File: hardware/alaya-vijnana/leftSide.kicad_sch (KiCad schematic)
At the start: 46 parts, among them J1 Bat, J2 USB_C_Receptacle_USB2.0_16P, SW1 Power_Switch, U1 nRF52840, U2 BQ24075RGT, U3 XC6220B331MR, X1 32.768kHz, Y1 32Mhz

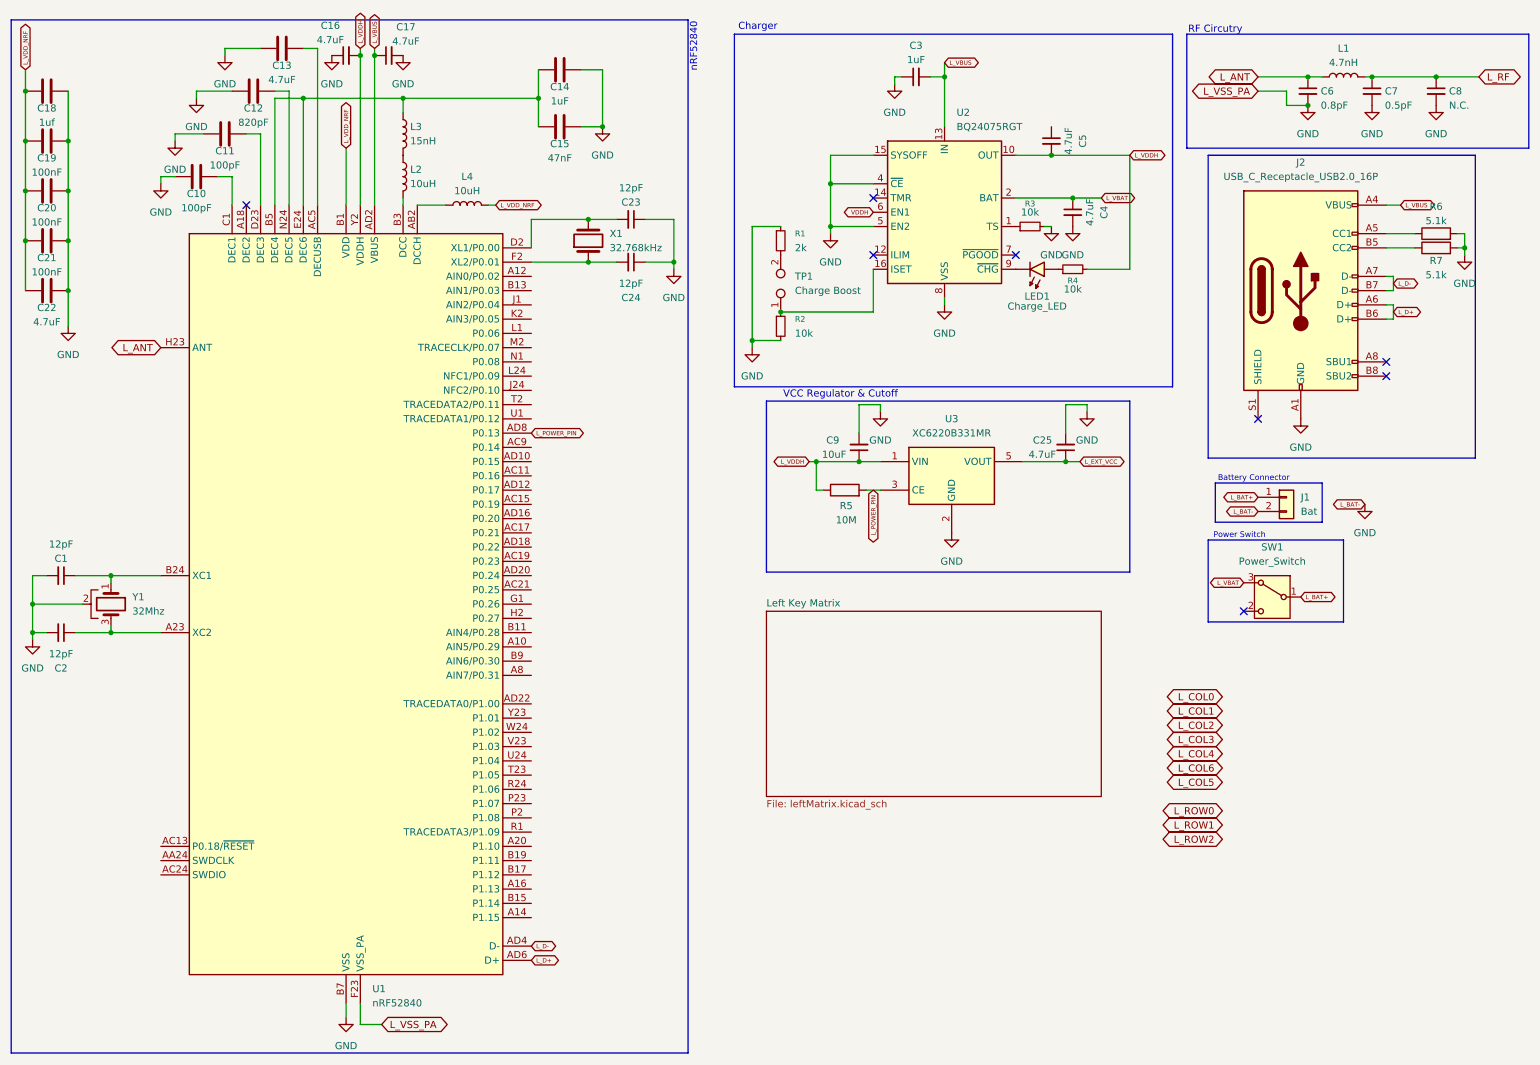
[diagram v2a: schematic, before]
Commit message: left side wired up
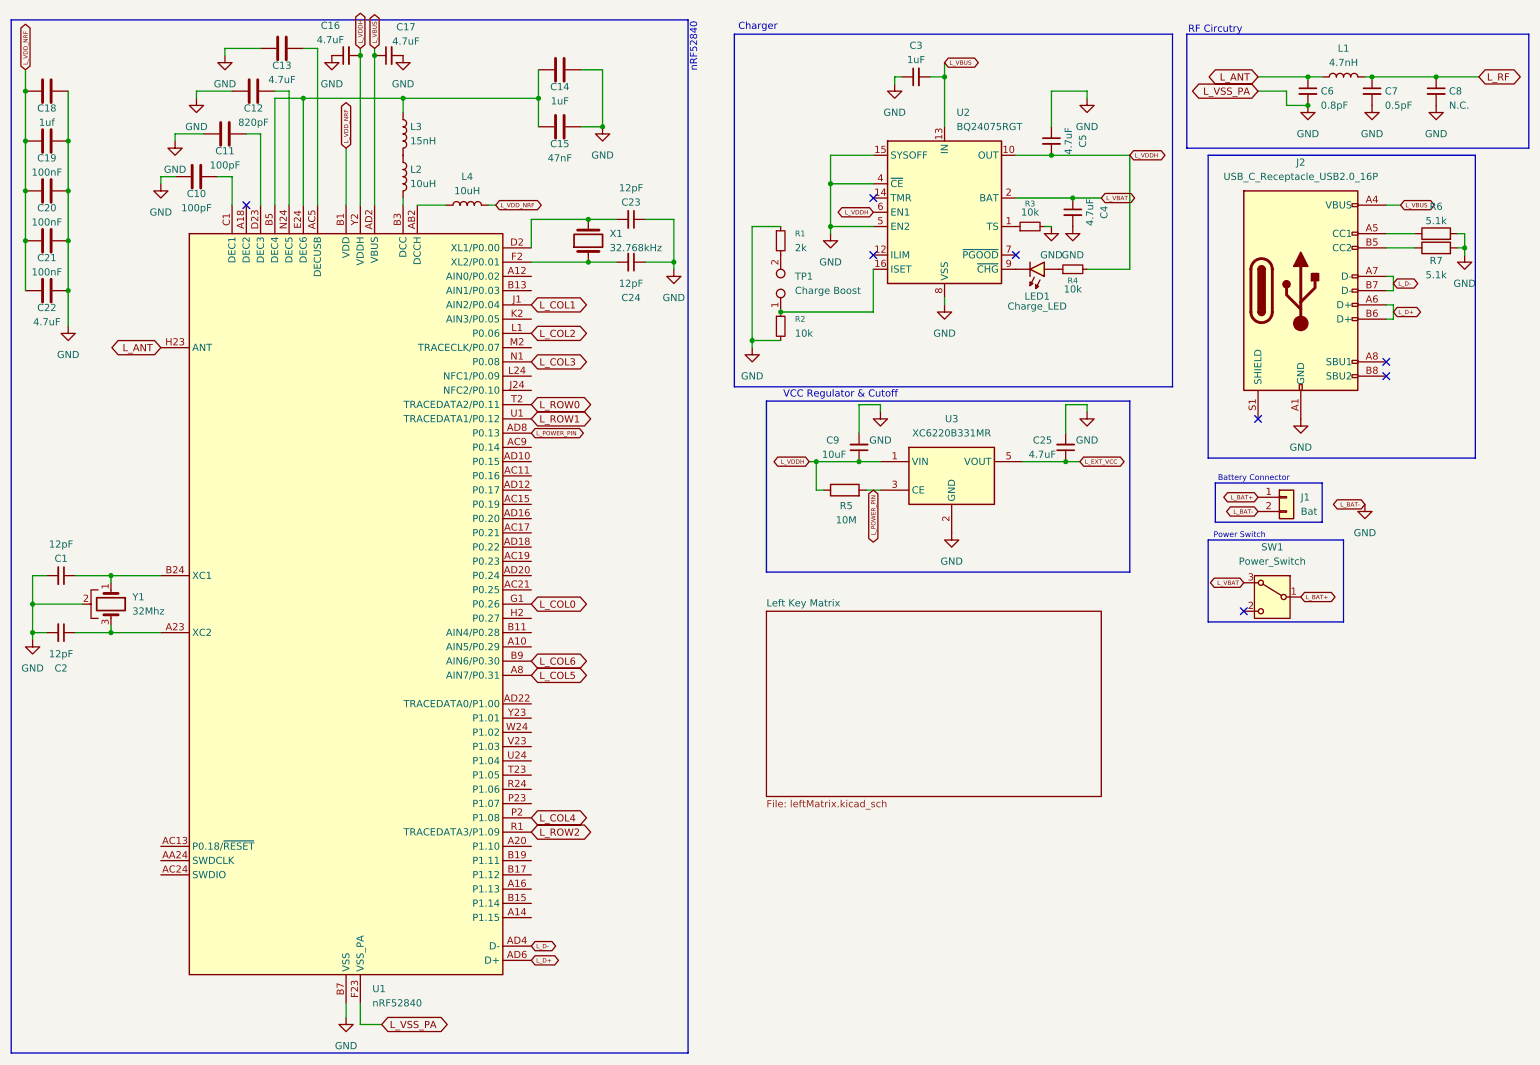
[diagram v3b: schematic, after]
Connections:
- net VDDH is gone; now on net L_VDDH: U2.6 (EN1)
- net GND: now also C5.1
- net L_COL0: now also U1.G1 (P0.26)
- net L_COL1: now also U1.J1 (AIN2/P0.04)
- net L_COL2: now also U1.L1 (P0.06)
- net L_COL3: now also U1.N1 (P0.08)
- net L_COL4: now also U1.P2 (P1.08)
- net L_COL5: now also U1.A8 (AIN7/P0.31)
- net L_COL6: now also U1.B9 (AIN6/P0.30)
- net L_ROW0: now also U1.T2 (TRACEDATA2/P0.11)
- net L_ROW1: now also U1.U1 (TRACEDATA1/P0.12)
- net L_ROW2: now also U1.R1 (TRACEDATA3/P1.09)
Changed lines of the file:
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@@
 	(wire
 		(pts
+			(xy 198.12 25.4) (xy 204.47 25.4)
+		)
+		(stroke
+			(width 0)
+			(type default)
+		)
+	)
+	(wire
+		(pts
 			(xy 114.3 31.75) (xy 118.11 31.75)
 		)
@@
 	(wire
 		(pts
+			(xy 198.12 31.75) (xy 198.12 25.4)
+		)
+		(stroke
+			(width 0)
+			(type default)
+		)
+	)
+	(wire
+		(pts
 			(xy 130.81 55.88) (xy 125.73 55.88)
 		)
@@
 	(wire
 		(pts
+			(xy 204.47 25.4) (xy 204.47 26.67)
+		)
+		(stroke
+			(width 0)
+			(type default)
+		)
+	)
+	(wire
+		(pts
 			(xy 30.48 121.92) (xy 30.48 120.65)
 		)
@@
 	(global_label "L_ROW2"
 		(shape bidirectional)
-		(at 228.6 158.75 180)
+		(at 105.41 157.48 0)
 		(fields_autoplaced yes)
 		(effects
@@
 				(size 1.27 1.27)
 			)
-			(justify right)
+			(justify left)
 		)
 		(property "Intersheetrefs" "${INTERSHEET_REFS}"
-			(at 217.2464 158.75 0)
+			(at 116.7636 157.48 0)
 			(effects
 				(font
 					(size 1.27 1.27)
 				)
-				(justify right)
+				(justify left)
 				(hide yes)
 			)
@@
 	(global_label "L_ROW1"
 		(shape bidirectional)
-		(at 228.6 156.21 180)
+		(at 105.41 83.82 0)
 		(fields_autoplaced yes)
 		(effects
@@
 				(size 1.27 1.27)
 			)
-			(justify right)
+			(justify left)
 		)
 		(property "Intersheetrefs" "${INTERSHEET_REFS}"
-			(at 217.2464 156.21 0)
+			(at 116.7636 83.82 0)
 			(effects
 				(font
 					(size 1.27 1.27)
 				)
-				(justify right)
+				(justify left)
 				(hide yes)
 			)
@@
 	(global_label "L_COL6"
 		(shape bidirectional)
-		(at 228.6 146.05 180)
+		(at 105.41 127 0)
 		(fields_autoplaced yes)
 		(effects
@@
 				(size 1.27 1.27)
 			)
-			(justify right)
+			(justify left)
 		)
 		(property "Intersheetrefs" "${INTERSHEET_REFS}"
-			(at 217.6697 146.05 0)
+			(at 116.3403 127 0)
 			(effects
 				(font
 					(size 1.27 1.27)
 				)
-				(justify right)
+				(justify left)
 				(hide yes)
 			)
@@
 	(global_label "L_COL5"
 		(shape bidirectional)
-		(at 228.6 148.59 180)
+		(at 105.41 129.54 0)
 		(fields_autoplaced yes)
 		(effects
@@
 				(size 1.27 1.27)
 			)
-			(justify right)
+			(justify left)
 		)
 		(property "Intersheetrefs" "${INTERSHEET_REFS}"
-			(at 217.6697 148.59 0)
+			(at 116.3403 129.54 0)
 			(effects
 				(font
 					(size 1.27 1.27)
 				)
-				(justify right)
+				(justify left)
 				(hide yes)
 			)
@@
 	(global_label "L_COL1"
 		(shape bidirectional)
-		(at 228.6 135.89 180)
+		(at 105.41 63.5 0)
 		(fields_autoplaced yes)
 		(effects
@@
 				(size 1.27 1.27)
 			)
-			(justify right)
+			(justify left)
 		)
 		(property "Intersheetrefs" "${INTERSHEET_REFS}"
-			(at 217.6697 135.89 0)
+			(at 116.3403 63.5 0)
 			(effects
 				(font
 					(size 1.27 1.27)
 				)
-				(justify right)
+				(justify left)
 				(hide yes)
 			)
@@
 	(global_label "L_COL2"
 		(shape bidirectional)
-		(at 228.6 138.43 180)
+		(at 105.41 68.58 0)
 		(fields_autoplaced yes)
 		(effects
@@
 				(size 1.27 1.27)
 			)
-			(justify right)
+			(justify left)
 		)
 		(property "Intersheetrefs" "${INTERSHEET_REFS}"
-			(at 217.6697 138.43 0)
+			(at 116.3403 68.58 0)
 			(effects
 				(font
 					(size 1.27 1.27)
 				)
-				(justify right)
+				(justify left)
 				(hide yes)
 			)
@@
 	(global_label "L_COL0"
 		(shape bidirectional)
-		(at 228.6 133.35 180)
+		(at 105.41 116.84 0)
 		(fields_autoplaced yes)
 		(effects
@@
 				(size 1.27 1.27)
 			)
-			(justify right)
+			(justify left)
 		)
 		(property "Intersheetrefs" "${INTERSHEET_REFS}"
-			(at 217.6697 133.35 0)
+			(at 116.3403 116.84 0)
 			(effects
 				(font
 					(size 1.27 1.27)
 				)
-				(justify right)
+				(justify left)
 				(hide yes)
 			)
@@
 		)
 	)
-	(global_label "VDDH"
+	(global_label "L_VDDH"
 		(shape bidirectional)
 		(at 166.37 46.99 180)
@@
 		)
 		(property "Intersheetrefs" "${INTERSHEET_REFS}"
-			(at 160.9364 46.99 0)
+			(at 159.7389 46.99 0)
 			(effects
 				(font
@@
 	(global_label "L_COL3"
 		(shape bidirectional)
-		(at 228.6 140.97 180)
+		(at 105.41 73.66 0)
 		(fields_autoplaced yes)
 		(effects
@@
 				(size 1.27 1.27)
 			)
-			(justify right)
+			(justify left)
 		)
 		(property "Intersheetrefs" "${INTERSHEET_REFS}"
-			(at 217.6697 140.97 0)
+			(at 116.3403 73.66 0)
 			(effects
 				(font
 					(size 1.27 1.27)
 				)
-				(justify right)
+				(justify left)
 				(hide yes)
 			)
@@
 	(global_label "L_ROW0"
 		(shape bidirectional)
-		(at 228.6 153.67 180)
+		(at 105.41 81.28 0)
 		(fields_autoplaced yes)
 		(effects
@@
 				(size 1.27 1.27)
 			)
-			(justify right)
+			(justify left)
 		)
 		(property "Intersheetrefs" "${INTERSHEET_REFS}"
-			(at 217.2464 153.67 0)
+			(at 116.7636 81.28 0)
 			(effects
 				(font
 					(size 1.27 1.27)
 				)
-				(justify right)
+				(justify left)
 				(hide yes)
 			)
@@
 	(global_label "L_COL4"
 		(shape bidirectional)
-		(at 228.6 143.51 180)
+		(at 105.41 154.94 0)
 		(fields_autoplaced yes)
 		(effects
@@
 				(size 1.27 1.27)
 			)
-			(justify right)
+			(justify left)
 		)
 		(property "Intersheetrefs" "${INTERSHEET_REFS}"
-			(at 217.6697 143.51 0)
+			(at 116.3403 154.94 0)
 			(effects
 				(font
 					(size 1.27 1.27)
 				)
-				(justify right)
+				(justify left)
 				(hide yes)
 			)
@@
 					(unit 1)
 				)
+			)
+		)
+	)
+	(symbol
+		(lib_id "power:GND")
+		(at 204.47 26.67 0)
+		(unit 1)
+		(exclude_from_sim no)
+		(in_bom yes)
+		(on_board yes)
+		(dnp no)
+		(fields_autoplaced yes)
+		(property "Reference" "#PWR052"
+			(at 204.47 33.02 0)
+			(effects
+				(font
+					(size 1.27 1.27)
+				)
+				(hide yes)
+			)
+		)
+		(property "Value" "GND"
+			(at 204.47 31.75 0)
+			(effects
+				(font
+					(size 1.27 1.27)
+				)
+			)
+		)
+		(property "Footprint" ""
+			(at 204.47 26.67 0)
+			(effects
+				(font
+					(size 1.27 1.27)
+				)
+				(hide yes)
+			)
+		)
+		(property "Datasheet" ""
+			(at 204.47 26.67 0)
+			(effects
+				(font
+					(size 1.27 1.27)
+				)
+				(hide yes)
+			)
+		)
+		(property "Description" "Power symbol creates a global label with name \"GND\" , ground"
+			(at 204.47 26.67 0)
+			(effects
+				(font
+					(size 1.27 1.27)
+				)
+				(hide yes)
+			)
+		)
+		(pin "1"
+		)
+		(instances
+			(project ""
+				(path "/a3984b5f-5482-487c-827c-93986b80e1c8/0dccec26-d854-49d3-8867-bf55eaef7f97"
+					(reference "#PWR052")
+					(unit 1)
+				)

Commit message: production stuff
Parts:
- added SW45: SW_Push, Button_Switch_SMD:SW_Push_1P1T_NO_CK_KMR2, symbol Switch:SW_Push
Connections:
- net GND: now also SW45.1
- net at U1.AC13 (P0.18/~{RESET}): now also SW45.2
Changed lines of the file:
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@@
+	)
+	(symbol
+		(lib_id "Switch:SW_Push")
+		(at 34.29 160.02 0)
+		(unit 1)
+		(exclude_from_sim no)
+		(in_bom yes)
+		(on_board yes)
+		(dnp no)
+		(fields_autoplaced yes)
+		(property "Reference" "SW45"
+			(at 34.29 152.4 0)
+			(effects
+				(font
+					(size 1.27 1.27)
+				)
+			)
+		)
+		(property "Value" "SW_Push"
+			(at 34.29 154.94 0)
+			(effects
+				(font
+					(size 1.27 1.27)
+				)
+			)
+		)
+		(property "Footprint" "Button_Switch_SMD:SW_Push_1P1T_NO_CK_KMR2"
+			(at 34.29 154.94 0)
+			(effects
+				(font
+					(size 1.27 1.27)
+				)
+				(hide yes)
+			)
+		)
+		(property "Datasheet" "~"
+			(at 34.29 154.94 0)
+			(effects
+				(font
+					(size 1.27 1.27)
+				)
+				(hide yes)
+			)
+		)
+		(property "Description" "Push button switch, generic, two pins"
+			(at 34.29 160.02 0)
+			(effects
+				(font
+					(size 1.27 1.27)
+				)
+				(hide yes)
+			)
+		)
+		(pin "2"
+		)
+		(pin "1"
+		)
+		(instances
+			(project ""
+				(path "/a3984b5f-5482-487c-827c-93986b80e1c8/0dccec26-d854-49d3-8867-bf55eaef7f97"
+					(reference "SW45")
+					(unit 1)
+				)
+			)
+		)
 	)
 	(symbol
@@
 					(unit 1)
 				)
+			)
+		)
+	)
+	(symbol
+		(lib_id "power:GND")
+		(at 29.21 160.02 0)
+		(unit 1)
+		(exclude_from_sim no)
+		(in_bom yes)
+		(on_board yes)
+		(dnp no)
+		(fields_autoplaced yes)
+		(property "Reference" "#PWR055"
+			(at 29.21 166.37 0)
+			(effects
+				(font
+					(size 1.27 1.27)
+				)
+				(hide yes)
+			)
+		)
+		(property "Value" "GND"
+			(at 29.21 165.1 0)
+			(effects
+				(font
+					(size 1.27 1.27)
+				)
+			)
+		)
+		(property "Footprint" ""
+			(at 29.21 160.02 0)
+			(effects
+				(font
+					(size 1.27 1.27)
+				)
+				(hide yes)
+			)
+		)
+		(property "Datasheet" ""
+			(at 29.21 160.02 0)
+			(effects
+				(font
+					(size 1.27 1.27)
+				)
+				(hide yes)
+			)
+		)
+		(property "Description" "Power symbol creates a global label with name \"GND\" , ground"
+			(at 29.21 160.02 0)
+			(effects
+				(font
+					(size 1.27 1.27)
+				)
+				(hide yes)
+			)
+		)
+		(pin "1"
+		)
+		(instances
+			(project ""
+				(path "/a3984b5f-5482-487c-827c-93986b80e1c8/0dccec26-d854-49d3-8867-bf55eaef7f97"
+					(reference "#PWR055")
+					(unit 1)
+				)
